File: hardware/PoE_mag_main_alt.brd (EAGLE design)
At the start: 99.1 x 78.7 mm, 64 parts, among them IC1 LD1117S33TR, IC2 DS1338, IC4 ATMEGA1284, IC5 MCP2200, IC6 TSR 1-2450, Q1 2N7002, X1 PWR, X2 JTAG, X3 USB, X6 MICRO-SD-SOCKETHIROSE-DM3D, Y1 32k768, Y2 16MHz, Y3 12MHz

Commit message: Add new board versions
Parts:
- added C21, C22, C28: 22p, SteveMarple:0805-HAND
- added C23, C24, C25, C26: 100n, SteveMarple:1206-HAND
- added C27, C29, C30, C31: 1u, SteveMarple:1206-HAND
- added DP1: BAS40-05, SteveMarple:SOT23-3-HAND
- added IC3, IC7, IC8, IC9: 74LVC1T45SOT23-HAND, SteveMarple:SOT23-6-HAND
- added JP10: CONFIG, pinhead:2X05
- added JP11: GPS !RESET! (A0), SparkFun:1X02
- added JP4: PPS 7/6, SparkFun:1X03
- added JP6: V ANT, SparkFun:1X03
- added L3: 47n, SteveMarple:0805-HAND
- added R11, R13: 10k, SteveMarple:1206-HAND
- added R12: 100k, SteveMarple:1206-HAND
- added RF1: NV08C-CSM, nvs-tech:NVC08C-CSM-HAND
- added U$16, U$18, U$19, U$21, U$22, U$23, U$24, U$25: PAD, SteveMarple:PAD
- added U$20: ?, SteveMarple:PAD
- added X4: CONN-SMATHD, SteveMarple:SMA-THD
- added X5: UFL, SteveMarple:CONN-UFL-HAND-SOLDERING
- moved BAT1 61.6 mm to (156.2, 68.6)
- moved C18 61.6 mm to (144.1, 27.3)
- moved C4 61.6 mm to (154.3, 35.6)
- moved C7 61.6 mm to (90.8, 78.1)
- moved D1 61.6 mm to (128.3, 76.2)
- moved H1 61.6 mm to (154.3, 19.7)
- moved H4 61.6 mm to (154.3, 89.5)
- moved IC2 61.6 mm to (149.9, 35.6)
- moved R4 61.6 mm to (144.1, 53.3)
- moved R7 61.6 mm to (154.3, 50.2)
- moved R8 61.6 mm to (154.3, 54.6)
- moved Y1 61.6 mm to (148.0, 29.2)
- moved C10 61.6 mm to (85.1, 78.1)
- moved C15 61.6 mm to (109.9, 33.7)
- moved C8 61.6 mm to (106.7, 40.3)
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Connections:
- new net !GPS_RESET: IC8.3, RF1.P$25
- new net GPIO0: RF1.P$20, U$18.1
- new net GPIO1: IC9.4, RF1.P$2, U$19.1
- new net GPIO2: RF1.P$1, U$20.1
- new net GPIO3: JP10.1, RF1.P$6, U$21.1
- new net GPIO4: JP10.3, RF1.P$7, U$22.1
- new net GPIO5: JP10.5, RF1.P$4, U$23.1
- new net GPIO6: JP10.7, RF1.P$35, U$24.1
- new net GPIO7: JP10.9, RF1.P$5, U$25.1
- new net GPS_RX1: IC7.3, RF1.P$33
- new net GPS_TX1: IC3.4, RF1.P$32
- new net N$22: IC8.4, JP11.2, R11.1
- new net N$23: C21.2, L3.2, X4.SIG, X5.SIGNAL
- new net N$24: C21.1, RF1.P$15
- new net N$25: IC3.3, R13.2
- new net PPS: IC9.3, JP4.2
- new net SLEEP_FLAG: RF1.P$21, U$16.1
- new net V_ANT: C22.1, JP6.2, L3.1
- new net V_BACKUP: DP1.3, RF1.P$23
- net +3V3: now also C25.1, C26.1, C27.1, C28.1, C29.1, C31.1, DP1.2, IC3.6, IC7.1, IC8.1, IC9.6, JP10.2, JP10.4, JP10.6, JP6.3, RF1.P$26, RF1.P$28, RF1.P$8
- net +5V: now also C30.1, JP6.1
- net 2(RX1): now also R13.1
- net 3(TX1): now also IC7.4, R12.1
- net 6: now also JP4.3
- net 7: now also JP4.1
- net A0: now also JP11.1
- net GND: now also C22.2, C23.2, C24.2, C25.2, C26.2, C27.2, C28.2, C29.2, C30.2, C31.2, IC3.2, IC3.5, IC7.2, IC7.5, IC8.2, IC8.5, IC9.2, IC9.5, JP10.10, JP10.8, RF1.P$10, RF1.P$11, RF1.P$12, RF1.P$13, RF1.P$14, RF1.P$16, RF1.P$17, RF1.P$18, RF1.P$19, RF1.P$22, RF1.P$24, RF1.P$27, RF1.P$29, RF1.P$3, RF1.P$34, RF1.P$9, X4.GND@0, X4.GND@1, X4.GND@2, X4.GND@3, X5.GND@0, X5.GND@1
- net VBATT: now also DP1.1
- net VCC: now also C23.1, C24.1, IC3.1, IC7.6, IC8.6, IC9.1, R11.2, R12.2
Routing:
- net GND: track 0.00 -> 198.9 mm, vias 0 -> 25
- net +3V3: track 0.00 -> 19.0 mm
- net N$23: track 0.00 -> 15.3 mm
- net GPIO3: track 0.00 -> 14.5 mm
- net GPIO7: track 0.00 -> 14.4 mm
- net GPIO1: track 0.00 -> 10.8 mm
- net GPIO4: track 0.00 -> 9.10 mm
- net GPIO5: track 0.00 -> 8.79 mm, vias 0 -> 1
- net GPIO2: track 0.00 -> 6.61 mm
- net N$24: track 0.00 -> 5.69 mm
- net SLEEP_FLAG: track 0.00 -> 4.49 mm
- net GPIO0: track 0.00 -> 3.76 mm
- net GPIO6: track 0.00 -> 2.54 mm
- net GPS_RX1: track 0.00 -> 1.74 mm
- net GPS_TX1: track 0.00 -> 1.46 mm
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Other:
- board size 99.1 x 78.7 mm -> 158.8 x 99.1 mm
- board text added: "3 H"
- board text added: "3V3/5V"
- board text added: "4 H"
- board text added: "5 H"
- board text added: "6 L"
- board text added: "7 L"
- board text added: "Arduino NV08C GPS Shield v1.0"
- board text added: "GPIO0"
- board text added: "GPIO1"
- board text added: "GPIO2"
- board text added: "SLEEP FLAG"
- board text added: "Steve Marple Lancaster University"

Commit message: Layout fixes
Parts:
- removed U$16, U$18, U$19, U$21, U$22, U$23, U$24, U$25: PAD, SteveMarple:PAD
- removed U$20: ?, SteveMarple:PAD
- added C32: 4u7, SteveMarple:CPOL-RADIAL-10UF-25V
- added C33, C34, C35, C36: 100n, SteveMarple:1206-HAND
- added U$10, U$2, U$3, U$4, U$6, U$7, U$8, U$9: PAD, SteveMarple:PAD
- added U$5: ?, SteveMarple:PAD
- moved JP4 91.9 mm to (105.4, 96.5), turned to 0 degrees
- moved C27 47.0 mm to (53.3, 8.89), turned to 270 degrees
- moved C29 45.2 mm to (47.6, 2.54), turned to 0 degrees
- moved C30 39.7 mm to (33.0, 34.0), turned to 180 degrees
- moved JP6 39.7 mm to (15.2, 40.6), turned to 180 degrees
- moved JP10 34.7 mm to (43.2, 38.1), turned to 0 degrees
- moved C26 31.4 mm to (14.0, 45.7)
- moved R13 31.0 mm to (55.9, 67.3), turned to 180 degrees
- moved X4 29.3 mm to (5.08, 14.0), turned to 270 degrees
- moved X5 26.4 mm to (12.7, 8.26), turned to 180 degrees
- moved C25 23.3 mm to (3.81, 53.3), turned to 90 degrees
- moved JP11 21.0 mm to (55.9, 71.1), turned to 180 degrees
- moved RF1 20.5 mm to (36.8, 17.8), turned to 180 degrees
- moved DP1 20.5 mm to (55.9, 3.81), turned to 180 degrees
- moved C23 18.8 mm to (24.1, 45.7)
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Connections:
- net +3V3: now also C30.1, C35.1, C36.1; no longer C31.1
- net +5V: no longer C30.1
- net GND: now also C32.2, C33.2, C34.2, C35.2, C36.2
- net GPIO0: now also U$3.1; no longer U$18.1
- net GPIO1: now also U$4.1; no longer U$19.1
- net GPIO2: now also U$5.1; no longer U$20.1
- net GPIO3: now also U$6.1; no longer U$21.1
- net GPIO4: now also U$7.1; no longer U$22.1
- net GPIO5: now also U$8.1; no longer U$23.1
- net GPIO6: now also U$9.1; no longer U$24.1
- net GPIO7: now also U$10.1; no longer U$25.1
- net SLEEP_FLAG: now also U$2.1; no longer U$16.1
- net VCC: now also C33.1, C34.1
- net V_ANT: now also C31.1, C32.1
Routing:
- net VCC: track 5.48 -> 4.86 mm
- net N$22: track 0.62 -> 0.00 mm
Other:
- outline, holes or cut-outs redrawn

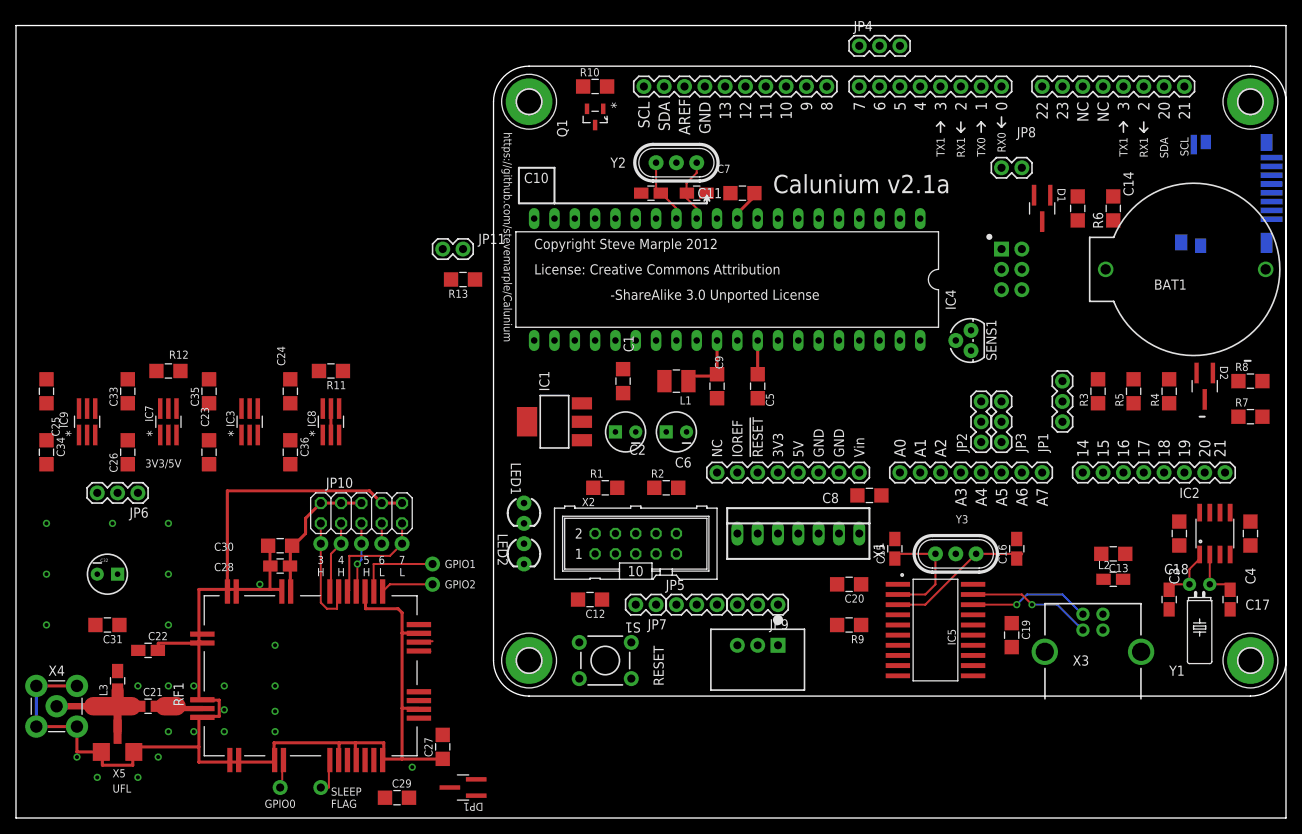
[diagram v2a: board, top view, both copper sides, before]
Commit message: Add magnetometer level shifting
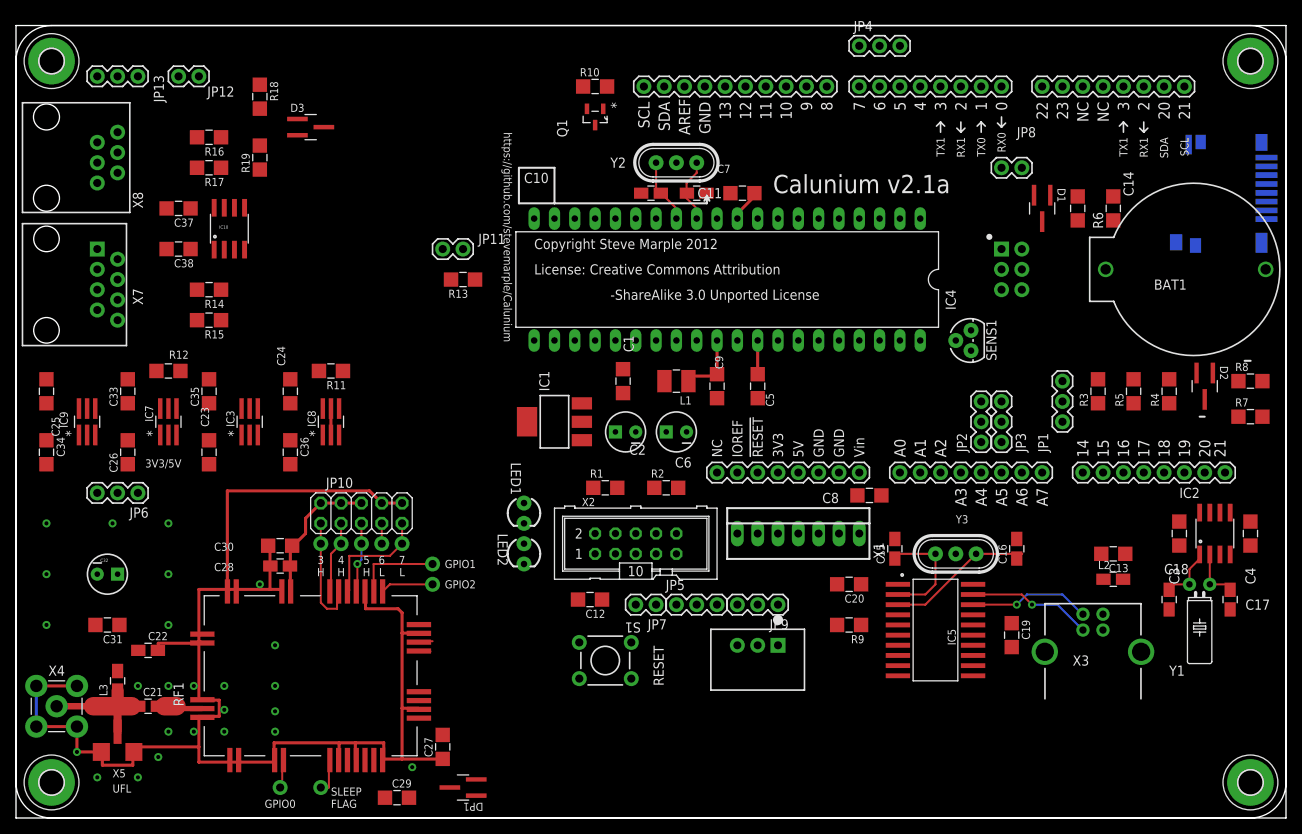
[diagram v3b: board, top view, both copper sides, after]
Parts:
- added C37, C38: 100n, SteveMarple:1206-HAND
- added D3: BAS40, SteveMarple:SOT23-3-HAND
- added IC10: PCA9517A, SteveMarple:SO08
- added JP12: 5V LINK, SparkFun:1X02
- added JP13: MAG VCC, SparkFun:1X03
- added R14, R15, R16, R17: 10k, SteveMarple:1206-HAND
- added R18: 3k, SteveMarple:1206-HAND
- added R19: 1k, SteveMarple:1206-HAND
- added X7: RJ45, SteveMarple:RJ45-8
- added X8: RJ11, SteveMarple:RJ11-6
- moved H2 61.6 mm to (4.45, 4.45)
- moved H3 59.9 mm to (4.45, 94.6)
- moved H1 15.2 mm to (154.3, 4.45)
- moved H4 5.08 mm to (154.3, 94.6)
- moved X6 0.63 mm to (154.9, 82.5)
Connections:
- new net MAG_SCL: IC10.7, R17.1, X7.5, X8.4
- new net MAG_SDA: IC10.6, R16.1, X7.7, X8.6
- new net MAG_VCC: C37.1, IC10.5, IC10.8, JP12.2, R16.2, R17.2, X7.6, X8.5
- new net N$26: JP13.2, X7.8
- net +3V3: now also JP13.3
- net +5V: now also JP12.1
- net 20(SDA): now also IC10.3, R15.1
- net 21(SCL): now also IC10.2, R14.1
- net A2: now also D3.1, R18.2, R19.2
- net GND: now also C37.2, C38.2, IC10.4, R19.1, X7.3, X7.4, X8.2, X8.3
- net VCC: now also C38.1, D3.3, IC10.1, R14.2, R15.2
- net VIN: now also JP13.1, R18.1, X7.2, X8.1
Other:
- outline, holes or cut-outs redrawn
- board text added: "+3V3"
- board text added: "VIN"

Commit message: Add schematics and boards for various modules
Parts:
- added D4: BAS21, SteveMarple:SOT23-3-HAND
- added Q2: BSS138, SteveMarple:SOT23-3-HAND
- added R20: 1M, SteveMarple:1206-HAND
- added R21: 330R, SteveMarple:1206-HAND
- added X9: 22-23-2021, con-molex:22-23-2021
- Q1: value 2N7002 -> BSS138; device SteveMarple:SOT23-3-ROTATED -> SteveMarple:SOT23-3-HAND
- moved R10 2.84 mm to (69.8, 92.7)
- moved Q1 2.54 mm to (69.8, 87.6)
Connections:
- new net N$27: D4.3, Q2.3, X9.2
- new net N$29: Q2.1, R20.2, R21.2
- net 8: now also R21.1
- net GND: now also D4.1, Q2.2, R20.1
- net VIN: now also X9.1

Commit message: Add Fibox box outline
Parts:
- added U$11: (no value), fibox:FIBOX-PC-M-95-G
- added U$12: (no value), fibox:PCB-150X150
- D1, D2: value BAT85 -> BAS40
- moved S1 8.89 mm to (73.7, 10.8)
- moved IC6 5.24 mm to (94.0, 16.5)
- moved JP4 1.27 mm to (105.4, 97.8)
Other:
- board size 158.8 x 99.1 mm -> 158.8 x 129.5 mm
- board text added: "AUTO RESET"

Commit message: Updates
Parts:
- removed Q2: BSS138, SteveMarple:SOT23-3-HAND
- removed U$11: (no value), fibox:FIBOX-PC-M-95-G
- removed U$12: (no value), fibox:PCB-150X150
- added BOX1: BOXFIBOX-PC-M-95-G, fibox:FIBOX-PC-M-95-G
- added Q3: BUK98150-55A, SteveMarple:SOT223-HAND
- moved R13 36.0 mm to (29.2, 43.2), turned to 0 degrees
- moved JP11 18.3 mm to (40.6, 61.0)
- moved JP6 16.3 mm to (2.54, 30.5), turned to 270 degrees
- moved D4 14.0 mm to (43.2, 86.4)
- moved D3 13.3 mm to (40.6, 73.7)
- moved R18 13.3 mm to (34.3, 77.5)
- moved R19 13.3 mm to (34.3, 69.8)
- moved R20 12.7 mm to (50.8, 92.7)
- moved R21 8.98 mm to (55.9, 81.3)
- moved BAT1 8.89 mm to (147.3, 68.6)
- moved C18 8.89 mm to (135.3, 27.3)
- moved C4 8.89 mm to (145.4, 35.6)
- moved D1 8.89 mm to (119.4, 76.2)
- moved D2 8.89 mm to (139.7, 54.0)
- moved H1 8.89 mm to (145.4, 4.45)
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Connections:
- net GND: now also Q3.3; no longer Q2.2
- net N$27: now also Q3.2, Q3.4; no longer Q2.3
- net N$29: now also Q3.1; no longer Q2.1
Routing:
- net GND: track 198.9 -> 193.9 mm
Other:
- board size 158.8 x 129.5 mm -> 149.9 x 129.5 mm

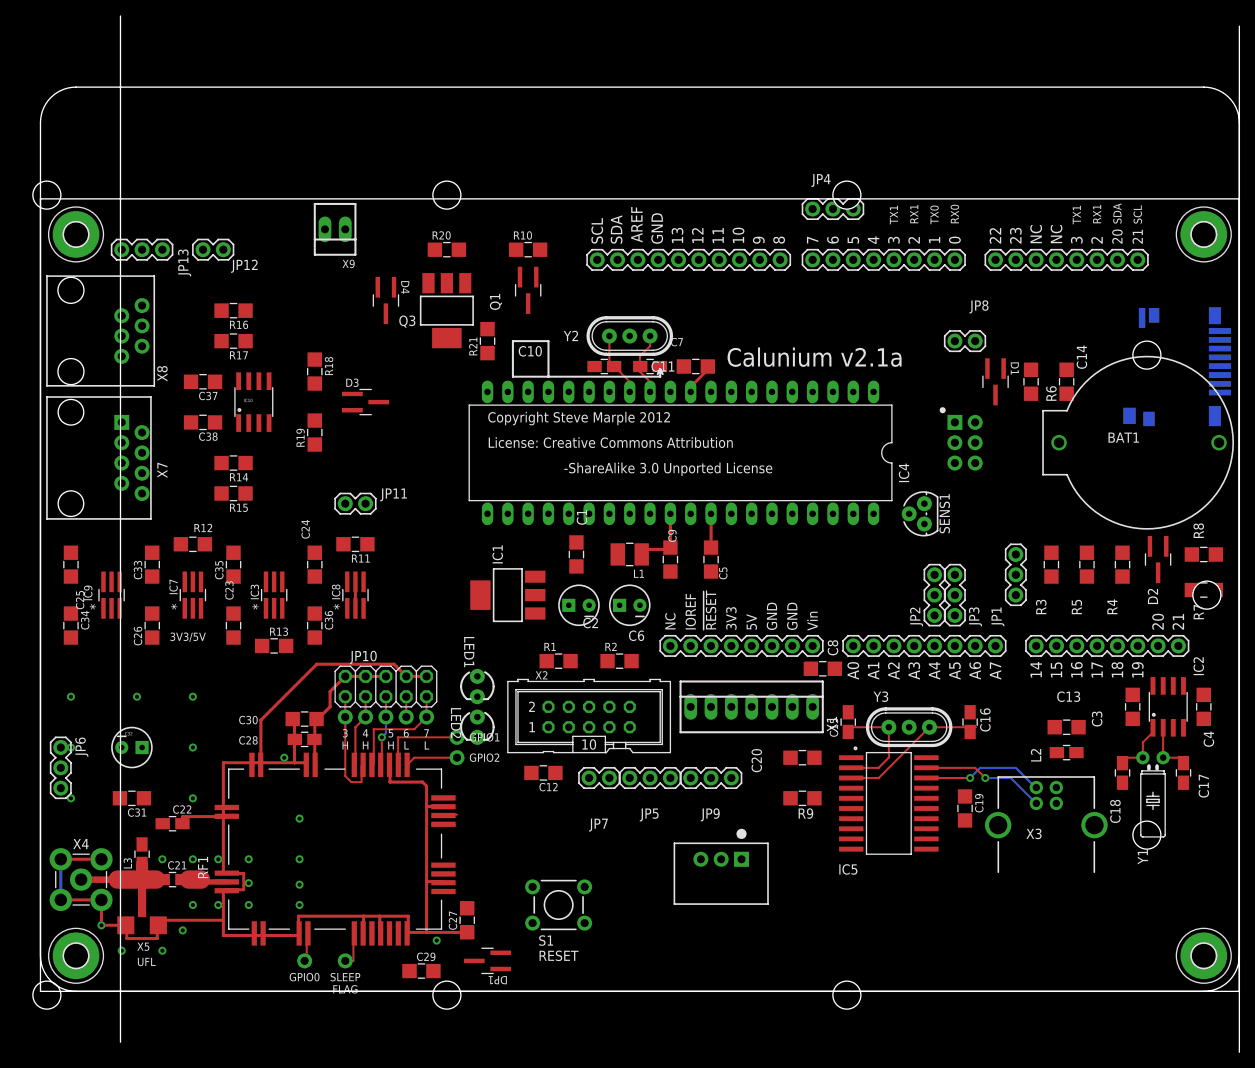
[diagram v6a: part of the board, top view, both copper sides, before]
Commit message: Update enclosure outline, move components
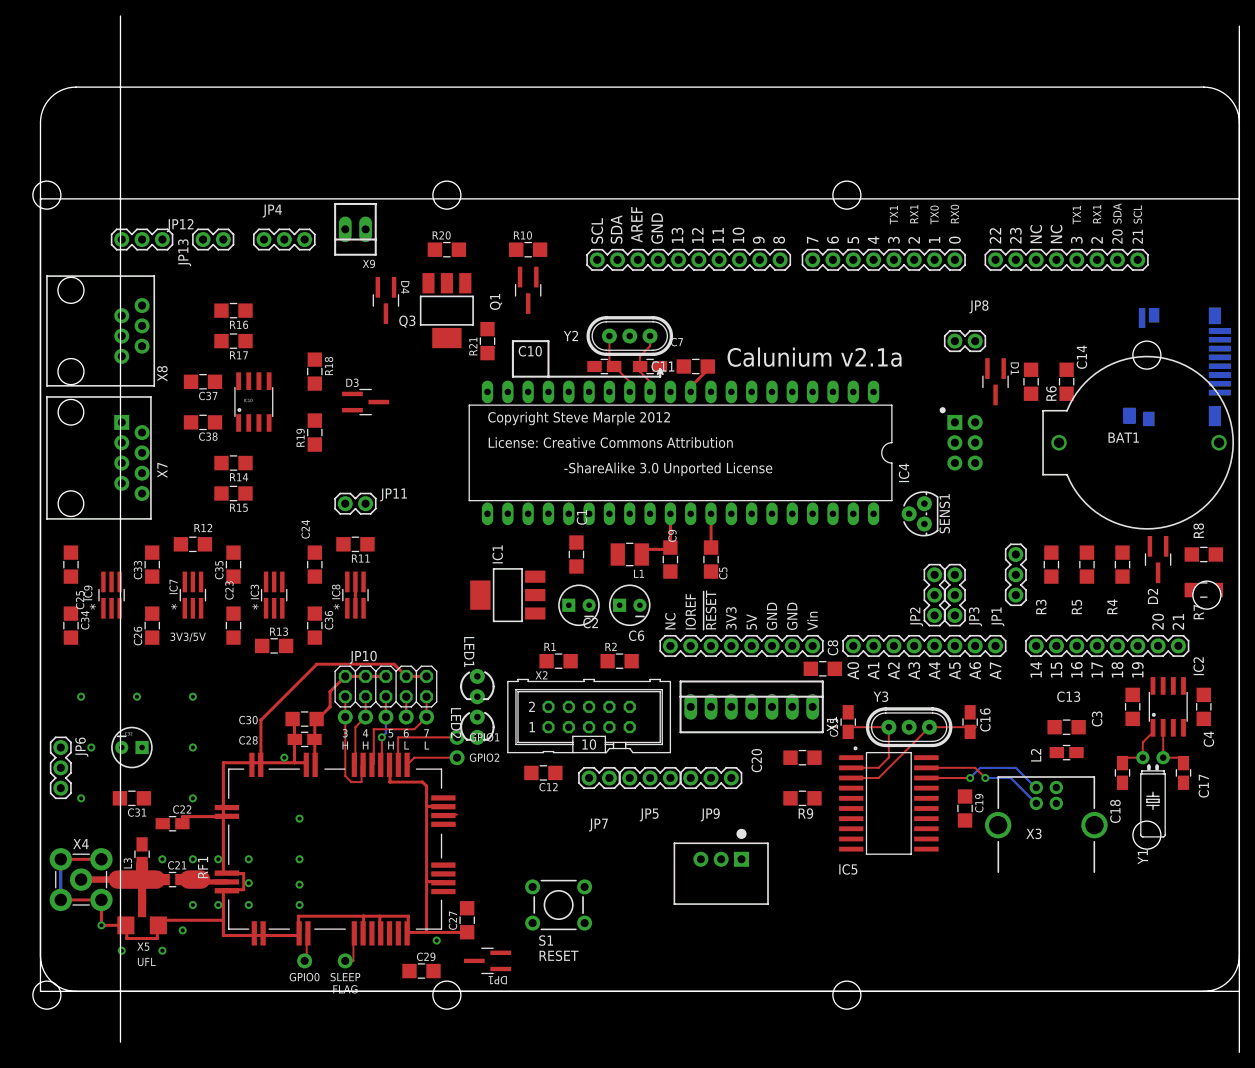
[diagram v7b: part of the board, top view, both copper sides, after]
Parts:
- removed H1, H2, H3, H4: (no value), holes:3,0-PAD
- R18: value 3k -> 3k 1%
- R19: value 1k -> 1k 1%
- moved JP4 68.7 mm to (27.9, 94.0)
- moved JP12 2.84 mm to (20.3, 94.0), turned to 0 degrees
- moved X9 2.54 mm to (39.4, 95.2)
- moved JP13 1.27 mm to (15.2, 94.0)
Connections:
- net GND: no longer H1.B3,0, H2.B3,0, H3.B3,0, H4.B3,0
